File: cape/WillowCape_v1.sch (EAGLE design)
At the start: 69 parts, among them U1 SN74LV245, U2 SN74LV245, U3 SN74LV245, U4 SN74LV245, U5 SN74LV245, U6 SN74LV245

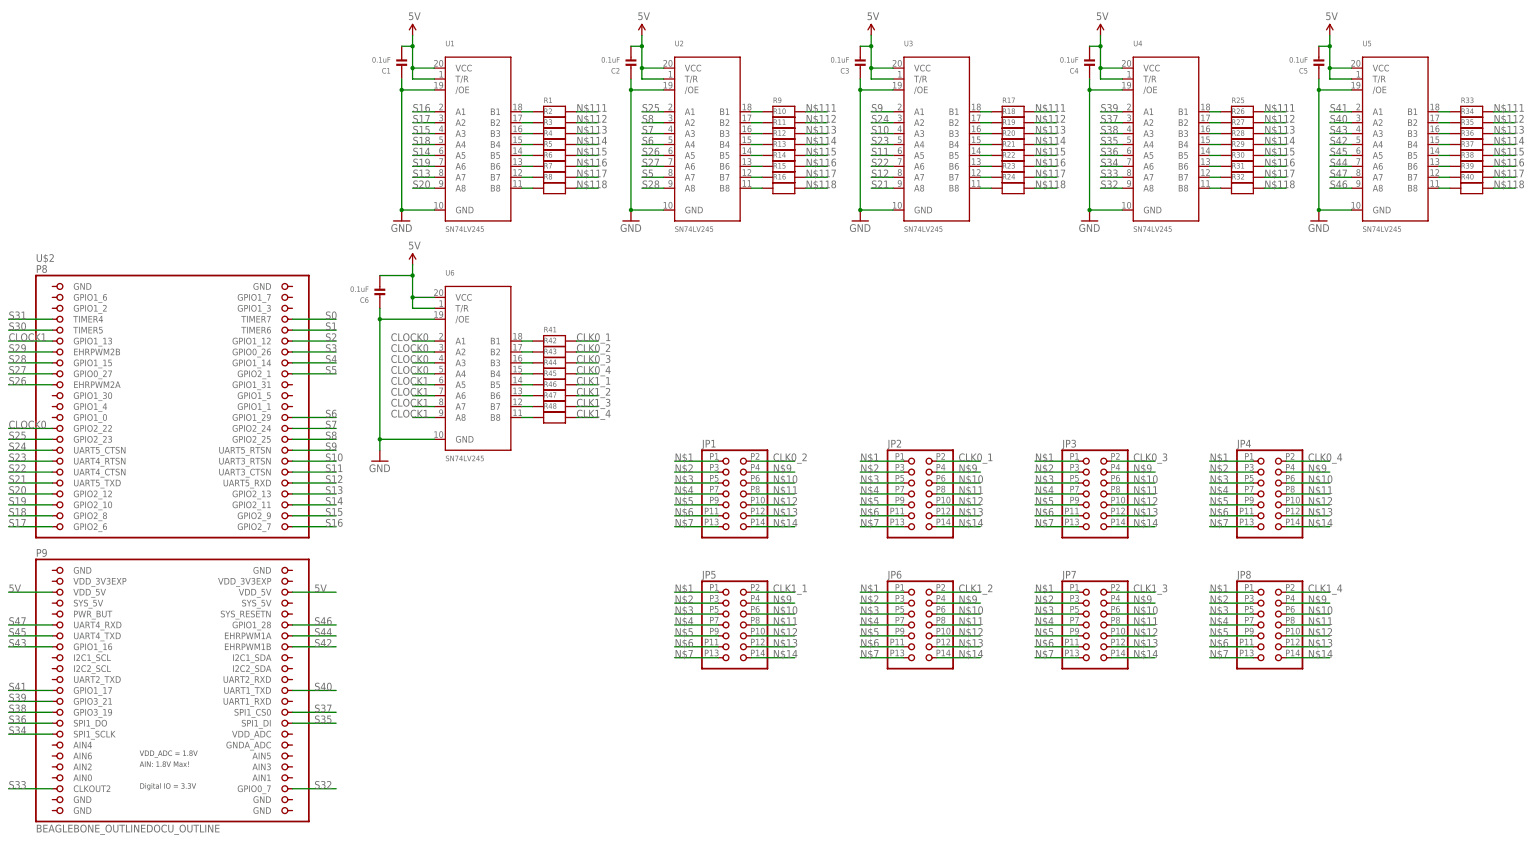
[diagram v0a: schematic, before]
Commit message: Done with v1 of control box. Motion sensors aren't connected yet but there are placeholders
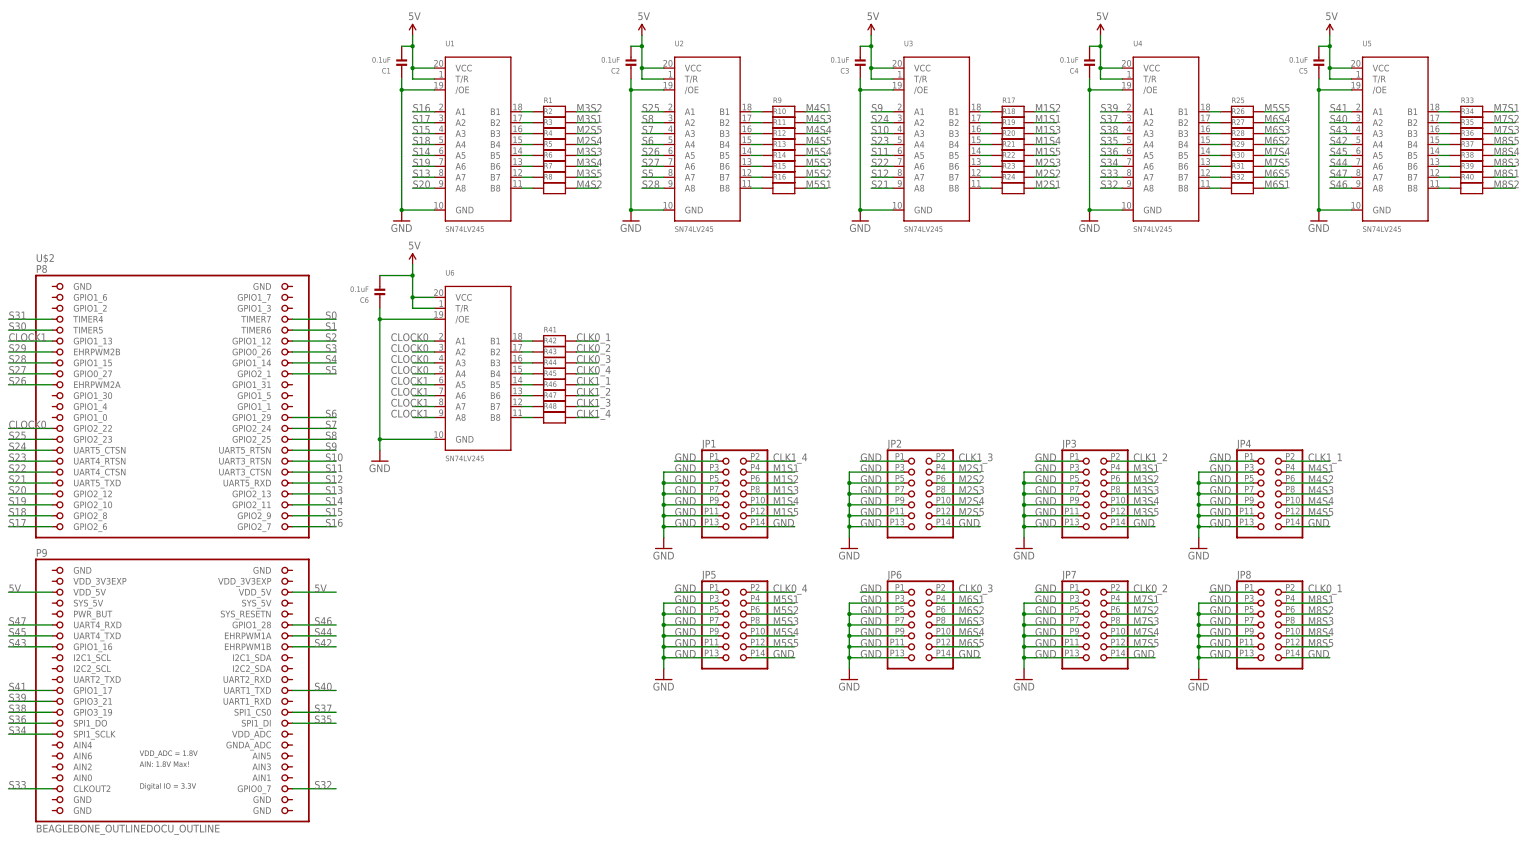
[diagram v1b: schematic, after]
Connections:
- removed net N$1: JP1.1, JP2.1, JP3.1, JP4.1, JP5.1, JP6.1, JP7.1, JP8.1
- removed net N$10: JP1.6, JP2.6, JP3.6, JP4.6, JP5.6, JP6.6, JP7.6, JP8.6
- removed net N$11: JP1.8, JP2.8, JP3.8, JP4.8, JP5.8, JP6.8, JP7.8, JP8.8
- removed net N$111: R1.2, R17.2, R25.2, R33.2, R9.2
- removed net N$112: R10.2, R18.2, R2.2, R26.2, R34.2
- removed net N$113: R11.2, R19.2, R27.2, R3.2, R35.2
- removed net N$114: R12.2, R20.2, R28.2, R36.2, R4.2
- removed net N$115: R13.2, R21.2, R29.2, R37.2, R5.2
- removed net N$116: R14.2, R22.2, R30.2, R38.2, R6.2
- removed net N$117: R15.2, R23.2, R31.2, R39.2, R7.2
- removed net N$118: R16.2, R24.2, R32.2, R40.2, R8.2
- removed net N$12: JP1.10, JP2.10, JP3.10, JP4.10, JP5.10, JP6.10, JP7.10, JP8.10
- removed net N$13: JP1.12, JP2.12, JP3.12, JP4.12, JP5.12, JP6.12, JP7.12, JP8.12
- removed net N$14: JP1.14, JP2.14, JP3.14, JP4.14, JP5.14, JP6.14, JP7.14, JP8.14
- removed net N$2: JP1.3, JP2.3, JP3.3, JP4.3, JP5.3, JP6.3, JP7.3, JP8.3
- removed net N$3: JP1.5, JP2.5, JP3.5, JP4.5, JP5.5, JP6.5, JP7.5, JP8.5
- removed net N$4: JP1.7, JP2.7, JP3.7, JP4.7, JP5.7, JP6.7, JP7.7, JP8.7
- removed net N$5: JP1.9, JP2.9, JP3.9, JP4.9, JP5.9, JP6.9, JP7.9, JP8.9
- removed net N$6: JP1.11, JP2.11, JP3.11, JP4.11, JP5.11, JP6.11, JP7.11, JP8.11
- removed net N$7: JP1.13, JP2.13, JP3.13, JP4.13, JP5.13, JP6.13, JP7.13, JP8.13
- removed net N$9: JP1.4, JP2.4, JP3.4, JP4.4, JP5.4, JP6.4, JP7.4, JP8.4
- new net M1S1: JP1.4, R18.2
- new net M1S2: JP1.6, R17.2
- new net M1S3: JP1.8, R19.2
- new net M1S4: JP1.10, R20.2
- new net M1S5: JP1.12, R21.2
- new net M2S1: JP2.4, R24.2
- new net M2S2: JP2.6, R23.2
- new net M2S3: JP2.8, R22.2
- new net M2S4: JP2.10, R4.2
- new net M2S5: JP2.12, R3.2
- new net M3S1: JP3.4, R2.2
- new net M3S2: JP3.6, R1.2
- new net M3S3: JP3.8, R5.2
- new net M3S4: JP3.10, R6.2
- new net M3S5: JP3.12, R7.2
- new net M4S1: JP4.4, R9.2
- new net M4S2: JP4.6, R8.2
- new net M4S3: JP4.8, R10.2
- new net M4S4: JP4.10, R11.2
- new net M4S5: JP4.12, R12.2
- new net M5S1: JP5.4, R16.2
- new net M5S2: JP5.6, R15.2
- new net M5S3: JP5.8, R14.2
- new net M5S4: JP5.10, R13.2
- new net M5S5: JP5.12, R25.2
- new net M6S1: JP6.4, R32.2
- new net M6S2: JP6.6, R28.2
- new net M6S3: JP6.8, R27.2
- new net M6S4: JP6.10, R26.2
- new net M6S5: JP6.12, R31.2
- new net M7S1: JP7.4, R33.2
- new net M7S2: JP7.6, R34.2
- new net M7S3: JP7.8, R35.2
- new net M7S4: JP7.10, R29.2
- new net M7S5: JP7.12, R30.2
- new net M8S1: JP8.4, R39.2
- new net M8S2: JP8.6, R40.2
- new net M8S3: JP8.8, R38.2
- new net M8S4: JP8.10, R37.2
- new net M8S5: JP8.12, R36.2
- net 5V: now also U2.T/R, U2.VCC
- net CLK0_1: now also JP8.2; no longer JP2.2
- net CLK0_2: now also JP7.2; no longer JP1.2
- net CLK0_3: now also JP6.2; no longer JP3.2
- net CLK0_4: now also JP5.2; no longer JP4.2
- net CLK1_1: now also JP4.2; no longer JP5.2
- net CLK1_2: now also JP3.2; no longer JP6.2
- net CLK1_3: now also JP2.2; no longer JP7.2
- net CLK1_4: now also JP1.2; no longer JP8.2
- net GND: now also JP1.1, JP1.11, JP1.13, JP1.14, JP1.3, JP1.5, JP1.7, JP1.9, JP2.1, JP2.11, JP2.13, JP2.14, JP2.3, JP2.5, JP2.7, JP2.9, JP3.1, JP3.11, JP3.13, JP3.14, JP3.3, JP3.5, JP3.7, JP3.9, JP4.1, JP4.11, JP4.13, JP4.14, JP4.3, JP4.5, JP4.7, JP4.9, JP5.1, JP5.11, JP5.13, JP5.14, JP5.3, JP5.5, JP5.7, JP5.9, JP6.1, JP6.11, JP6.13, JP6.14, JP6.3, JP6.5, JP6.7, JP6.9, JP7.1, JP7.11, JP7.13, JP7.14, JP7.3, JP7.5, JP7.7, JP7.9, JP8.1, JP8.11, JP8.13, JP8.14, JP8.3, JP8.5, JP8.7, JP8.9
